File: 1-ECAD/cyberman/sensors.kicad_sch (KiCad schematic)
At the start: 19 parts, among them J3 532610271, U11 LSM6DSOTR, U12 ICS-43434, U13 MAX98357A, U20 LIS2MDLTR

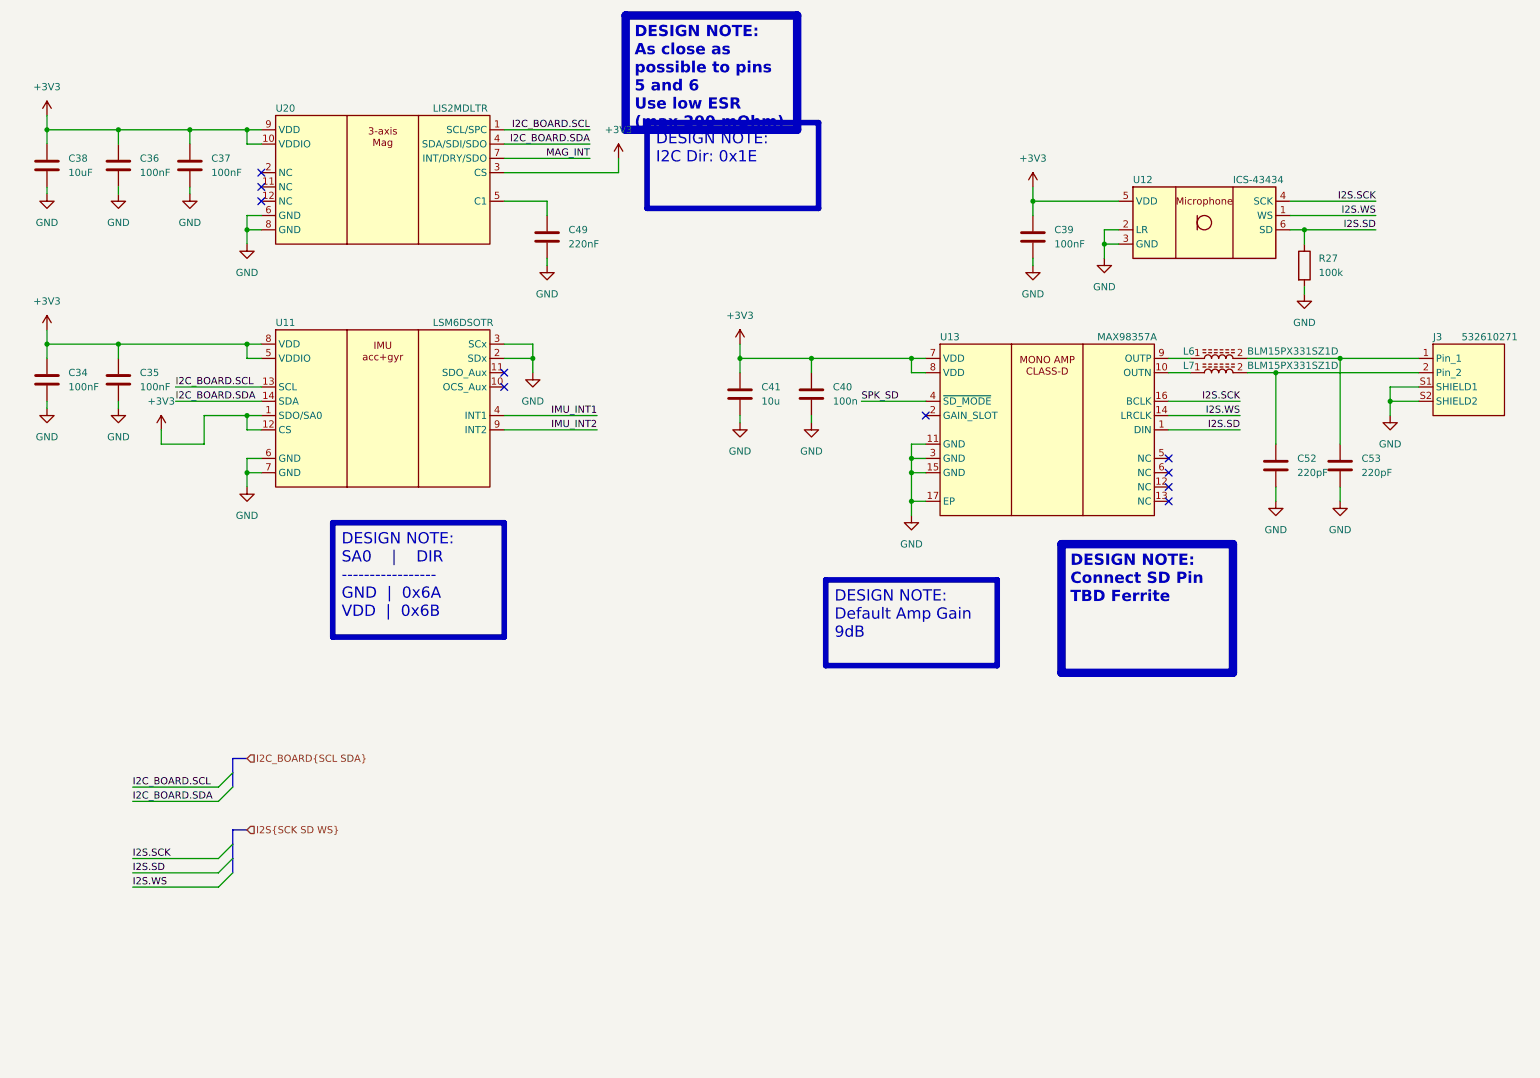
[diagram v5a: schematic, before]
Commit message: sensor page closed
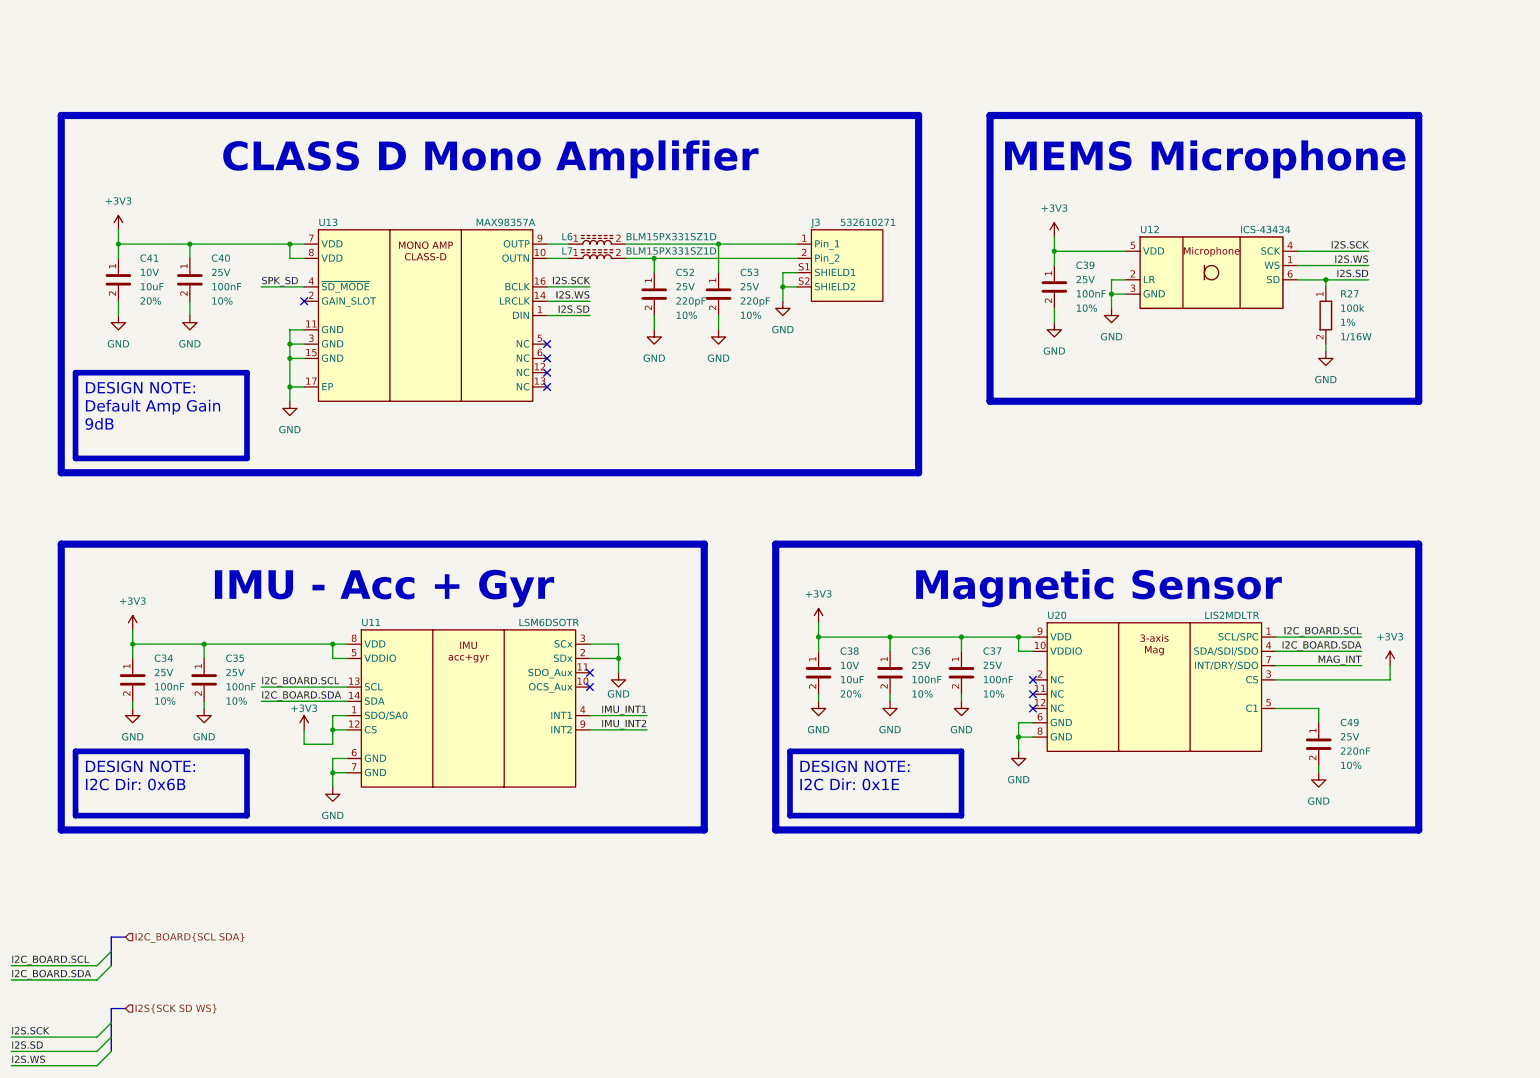
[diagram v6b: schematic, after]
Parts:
- removed C34, C35, C36, C37, C39: 100nF, symbol Device:C
- removed C38: 10uF, symbol Device:C
- removed C40: 100n, symbol Device:C
- removed C41: 10u, symbol Device:C
- removed C49: 220nF, symbol Device:C
- removed C52, C53: 220pF, symbol Device:C
- removed R27: 100k, symbol Device:R
- added C34, C35, C36, C37, C39, C40: CC0402KRX7R8BB104, 0_capacitor_smd:C_0402, symbol 0_capacitor_smd:CC0402KRX7R8BB104
- added C38, C41: CC0402MRX5R6BB106, 0_capacitor_smd:C_0402, symbol 0_capacitor_smd:CC0402MRX5R6BB106
- added C49: CC0402KRX5R8BB224, 0_capacitor_smd:C_0402, symbol 0_capacitor_smd:CC0402KRX5R8BB224
- added C52, C53: CC0402KRX7R8BB221, 0_capacitor_smd:C_0402, symbol 0_capacitor_smd:CC0402KRX7R8BB221
- added R27: RC0402FR-07100KL, 0_resistor_smd:R_0402, symbol 0_resistor_smd:RC0402FR-07100KL
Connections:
- net +3V3: now also C34.1, C35.1, C36.1, C37.1, C38.1, C39.1, C40.1, C41.1
- net GND: now also C34.2, C35.2, C36.2, C37.2, C38.2, C39.2, C40.2, C41.2, C49.2, C52.2, C53.2, R27.2
- net I2S.SD: now also R27.1
- net at J3.1 (Pin_1), L6.2: now also C53.1
- net at U20.5 (C1): now also C49.1
- net at J3.2 (Pin_2), L7.2: now also C52.1
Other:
- note added: "CLASS D Mono Amplifier"
- note added: "IMU - Acc + Gyr"
- note added: "MEMS Microphone"
- note added: "Magnetic Sensor"
- moved on the sheet: J3, L6, L7, U11, U12, U13, U20

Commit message: new changes
close display page and peripheral schematic
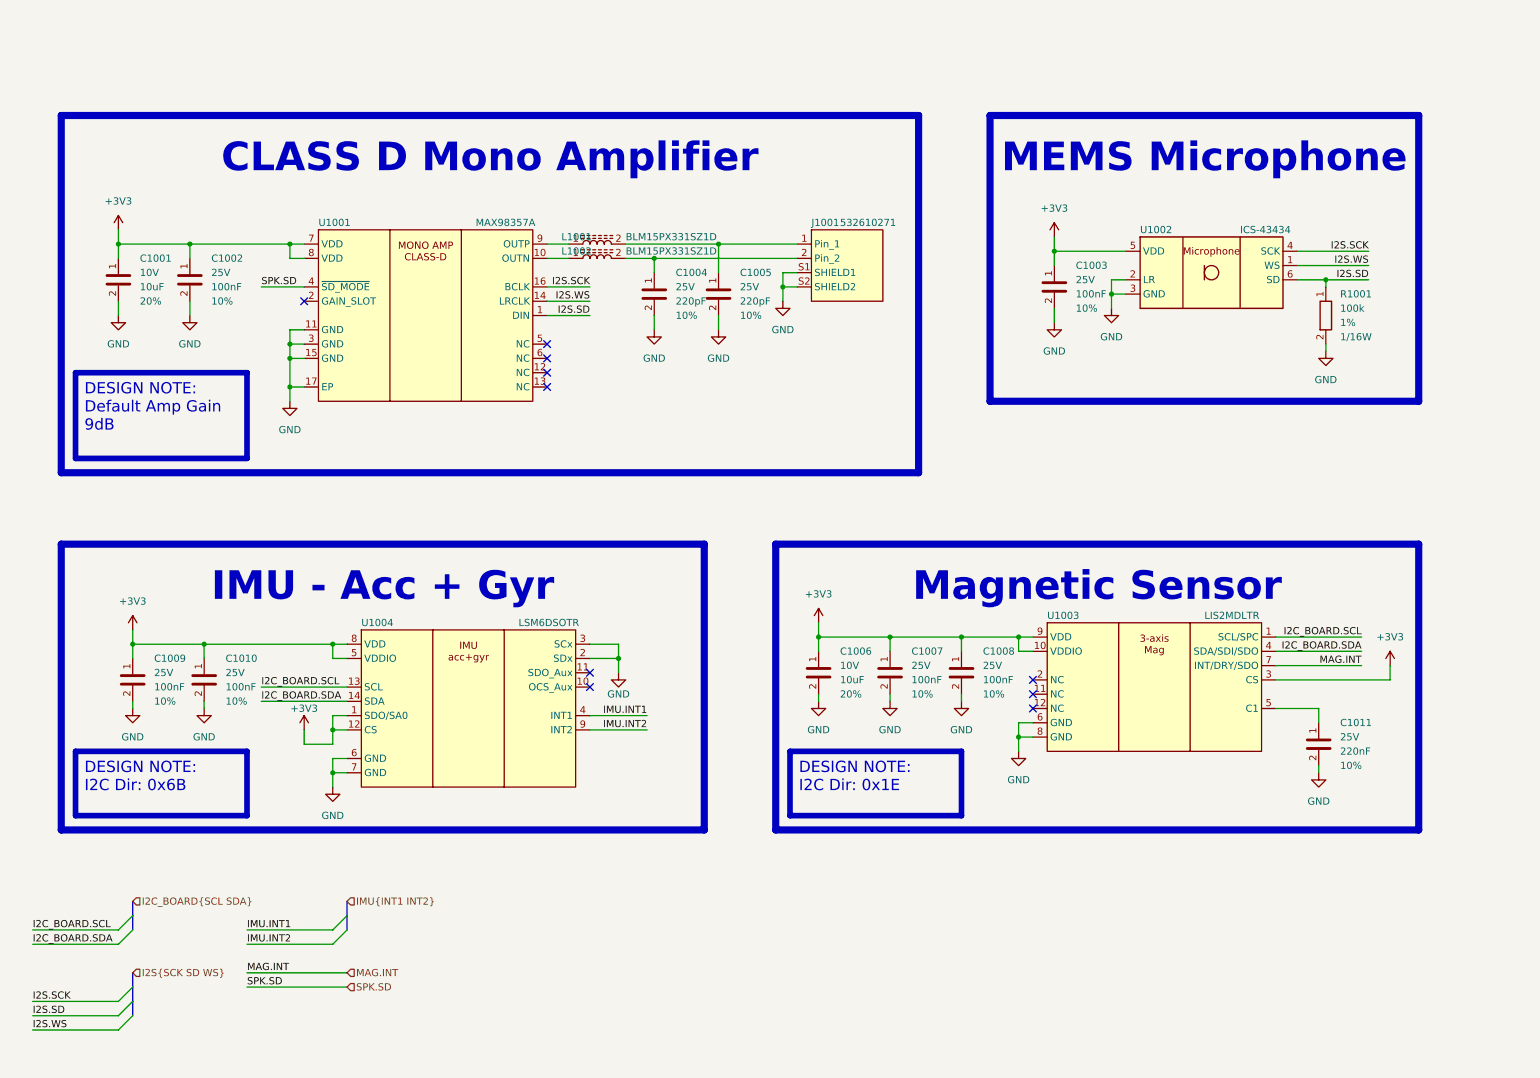
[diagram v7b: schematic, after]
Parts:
- renumbered C41 to C1001, C40 to C1002, C39 to C1003, C52 to C1004, C53 to C1005, C38 to C1006, C36 to C1007, C37 to C1008, C34 to C1009, C35 to C1010, C49 to C1011, J3 to J1001, L6 to L1001, L7 to L1002, R27 to R1001, U13 to U1001, U12 to U1002, U20 to U1003, U11 to U1004
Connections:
- net IMU_INT1 renamed IMU.INT1
- net IMU_INT2 renamed IMU.INT2
- net MAG_INT renamed MAG.INT
- net SPK_SD renamed SPK.SD
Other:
- company: (none) -> kode.
